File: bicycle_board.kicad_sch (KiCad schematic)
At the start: 47 parts, among them J1 Conn_02x05_Odd_Even, J10 USB_A, J11 Conn_01x02, J12 Conn_01x04, J13 Conn_01x04, J2 USB_C_Receptacle_USB2.0_16P, J5 Micro_SD_Card, J6 Conn_01x08, J7 Conn_01x03, J8 Conn_01x02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

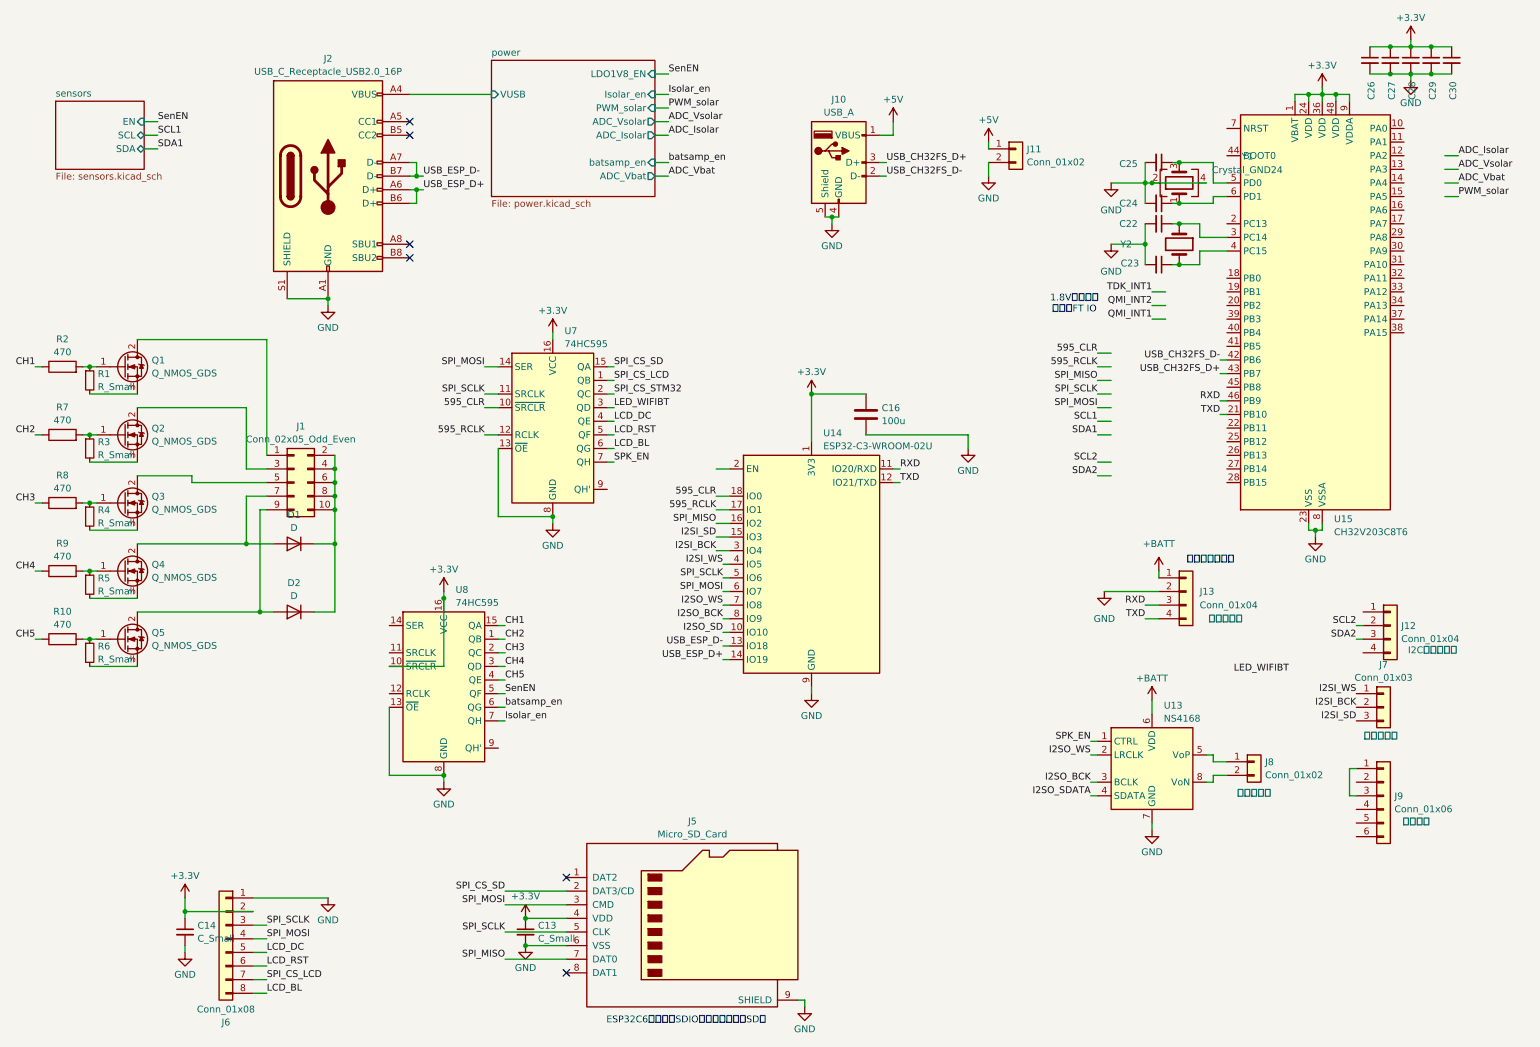
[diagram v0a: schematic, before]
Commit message: MOS管修改为GSD, 添加芯片附近滤波电容、上拉电阻等，调整模块间布局，改正AHT20封装，电解电容替换成1210 MLCC
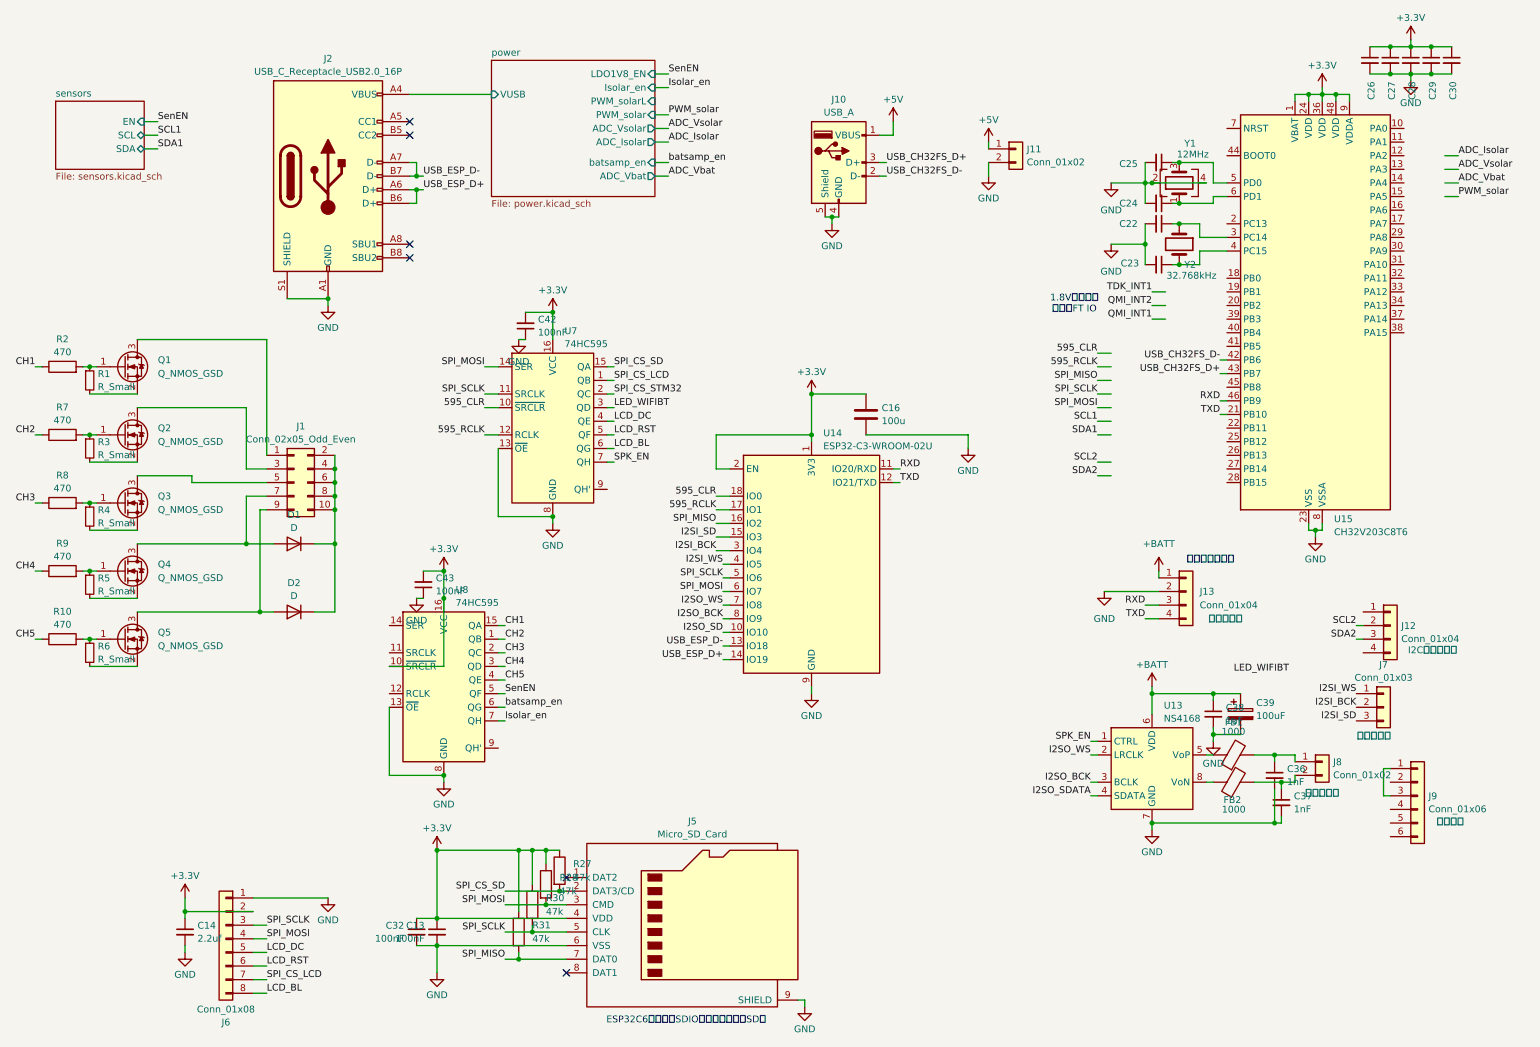
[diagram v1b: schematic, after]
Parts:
- added C32, C42, C43: 100nF, Capacitor_SMD:C_0402_1005Metric, symbol Device:C_Small
- added C36, C37: 1nF, Capacitor_SMD:C_0402_1005Metric, symbol Device:C_Small
- added C38: 1uF, Capacitor_SMD:C_0402_1005Metric, symbol Device:C_Small
- added C39: 100uF, Capacitor_SMD:C_1210_3225Metric, symbol Device:C_Polarized
- added FB1, FB2: 1000, Inductor_SMD:L_0805_2012Metric, symbol Device:FerriteBead
- added R27, R28, R30, R31: 47k, Resistor_SMD:R_0402_1005Metric, symbol Device:R
- C13, C26, C27, C28, C29, C30: value C_Small -> 100nF
- C14: value C_Small -> 2.2uf; footprint Capacitor_SMD:C_0402_1005Metric -> Capacitor_SMD:C_0603_1608Metric
- Q1, Q2, Q3, Q4, Q5: value Q_NMOS_GDS -> Q_NMOS_GSD; symbol Device:Q_NMOS_GDS -> Device:Q_NMOS_GSD
- Y1: value Crystal_GND24 -> 12MHz
- Y2: value Crystal -> 32.768kHz
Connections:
- net +3.3V: now also U14.2 (EN), C32.1, C42.2, C43.2, R27.1, R28.1, R30.1, R31.1
- net +BATT: now also C38.1, C39.1
- net GND: now also C32.2, C36.2, C37.2, C38.2, C39.2, C42.1, C43.1
- net SPI_CS_SD: now also R27.2
- net SPI_MISO: now also R31.2
- net SPI_MOSI: now also R28.2
- net SPI_SCLK: now also R30.2
- net at R1.2: now also Q1.2 (S); no longer Q1.3 (S)
- net at D1.2 (A), J1.7 (Pin_7): now also Q4.3 (D); no longer Q4.2 (D)
- net at R6.2: now also Q5.2 (S); no longer Q5.3 (S)
- net at Q3.2 (S): now also R4.2; no longer J1.5 (Pin_5)
- net at Q3.3 (D): now also J1.5 (Pin_5); no longer R4.2
- net at J1.1 (Pin_1): now also Q1.3 (D); no longer Q1.2 (D)
- net at R5.2: now also Q4.2 (S); no longer Q4.3 (S)
- net at U13.5 (VoP): now also FB1.1; no longer J8.1 (Pin_1)
- net at U13.8 (VoN): now also FB2.1; no longer J8.2 (Pin_2)
- net at D2.2 (A), J1.9 (Pin_9): now also Q5.3 (D); no longer Q5.2 (D)
- net at R3.2: now also Q2.2 (S); no longer Q2.3 (S)
- net at J1.3 (Pin_3): now also Q2.3 (D); no longer Q2.2 (D)
- new net: C37.1, FB2.2, J8.2 (Pin_2)
- new net: C36.1, FB1.2, J8.1 (Pin_1)
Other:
- sheet power ports: added PWM_solarL; removed none
- moved on the sheet: C13, J8, J9

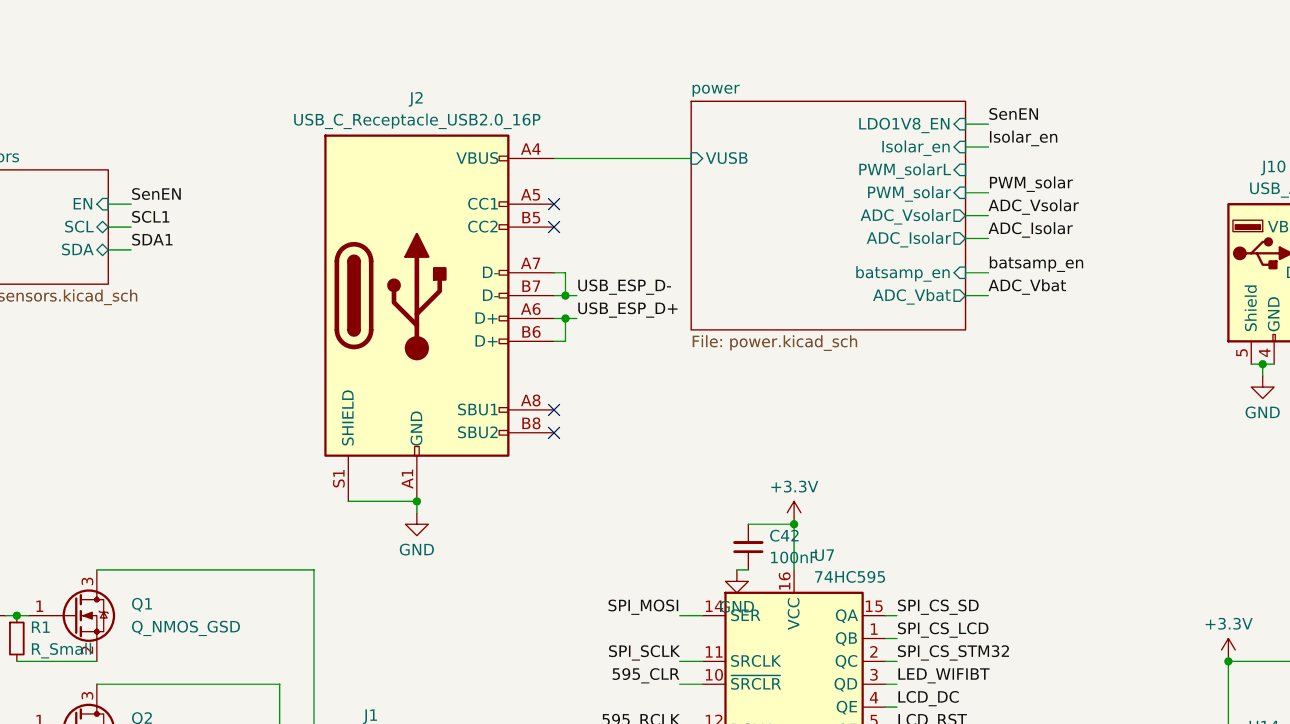
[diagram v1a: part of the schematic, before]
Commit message: 添加升压USB 5V输出
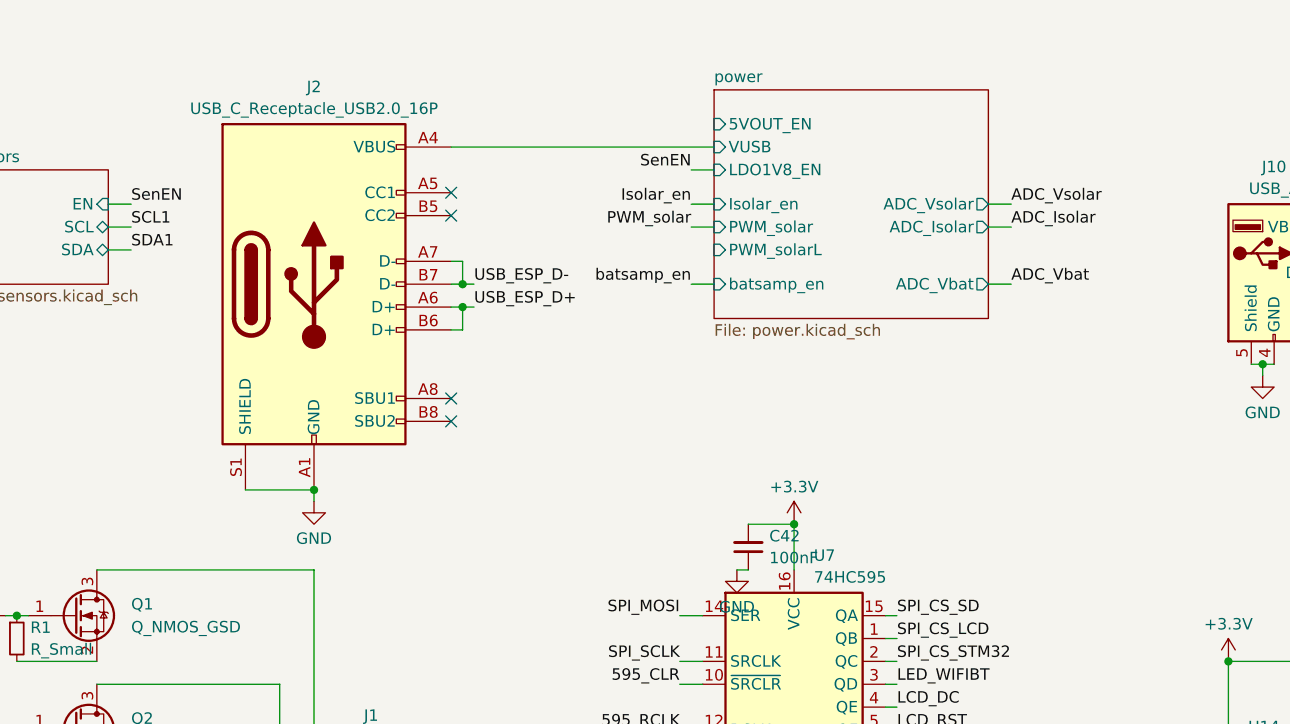
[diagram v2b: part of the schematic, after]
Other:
- sheet power ports: added 5VOUT_EN; removed none
- moved on the sheet: J2

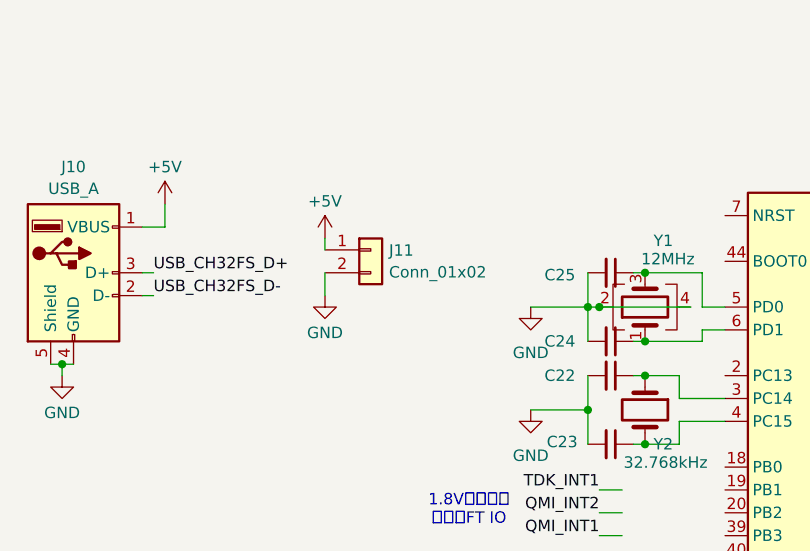
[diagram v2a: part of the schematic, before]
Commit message: 初步划定PCB边缘，改为紧凑布局
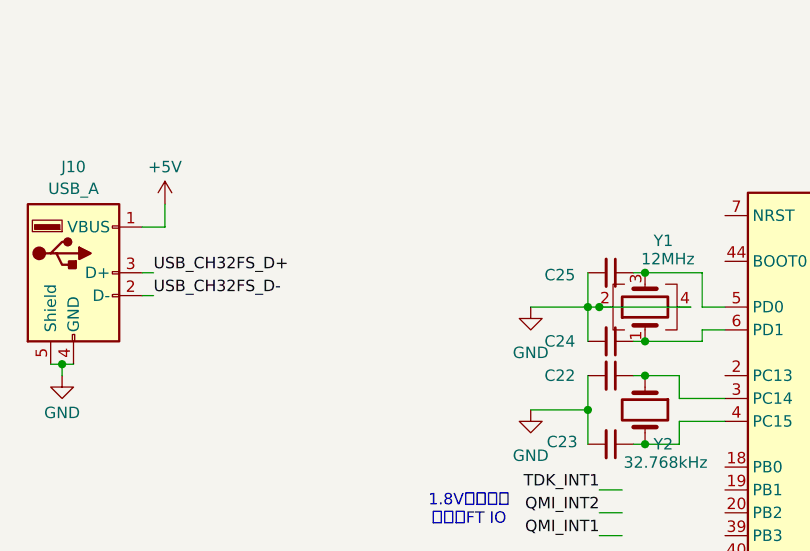
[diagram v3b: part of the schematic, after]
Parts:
- removed J11: Conn_01x02, Connector_PinHeader_2.54mm:PinHeader_1x02_P2.54mm_Vertical, symbol Connector_Generic:Conn_01x02
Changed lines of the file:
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@@
 	(wire
 		(pts
-			(xy 196.85 31.75) (xy 196.85 33.02)
-		)
-		(stroke
-			(width 0)
-			(type default)
-		)
-	)
-	(wire
-		(pts
 			(xy 238.76 146.05) (xy 237.49 146.05)
 		)
@@
 	(wire
 		(pts
-			(xy 196.85 35.56) (xy 196.85 38.1)
-		)
-		(stroke
-			(width 0)
-			(type default)
-		)
-	)
-	(wire
-		(pts
 			(xy 167.64 45.72) (xy 167.64 46.99)
 		)
@@
 	)
 	(symbol
-		(lib_id "Connector_Generic:Conn_01x02")
-		(at 201.93 33.02 0)
-		(unit 1)
-		(exclude_from_sim no)
-		(in_bom yes)
-		(on_board yes)
-		(dnp no)
-		(fields_autoplaced yes)
-		(property "Reference" "J11"
-			(at 203.962 33.0778 0)
-			(effects
-				(font
-					(size 1.27 1.27)
-				)
-				(justify left)
-			)
-		)
-		(property "Value" "Conn_01x02"
-			(at 203.962 35.5021 0)
-			(effects
-				(font
-					(size 1.27 1.27)
-				)
-				(justify left)
-			)
-		)
-		(property "Footprint" "Connector_PinHeader_2.54mm:PinHeader_1x02_P2.54mm_Vertical"
-			(at 201.93 33.02 0)
-			(effects
-				(font
-					(size 1.27 1.27)
-				)
-				(hide yes)
-			)
-		)
-		(property "Datasheet" "~"
-			(at 201.93 33.02 0)
-			(effects
-				(font
-					(size 1.27 1.27)
-				)
-				(hide yes)
-			)
-		)
-		(property "Description" "5V电源输出"
-			(at 201.93 33.02 0)
-			(effects
-				(font
-					(size 1.27 1.27)
-				)
-				(hide yes)
-			)
-		)
-		(property "Sim.Type" ""
-			(at 201.93 33.02 0)
-			(effects
-				(font
-					(size 1.27 1.27)
-				)
-				(hide yes)
-			)
-		)
-		(pin "2"
-		)
-		(pin "1"
-		)
-		(instances
-			(project ""
-				(path "/a369956d-4c9f-46c3-810f-e3e9616ab1a2"
-					(reference "J11")
-					(unit 1)
-				)
-			)
-		)
-	)
-	(symbol
 		(lib_id "RF_Module:ESP32-C3-WROOM-02U")
 		(at 163.83 110.49 0)
@@
 	)
 	(symbol
-		(lib_id "power:GND")
-		(at 196.85 38.1 0)
-		(unit 1)
-		(exclude_from_sim no)
-		(in_bom yes)
-		(on_board yes)
-		(dnp no)
-		(fields_autoplaced yes)
-		(property "Reference" "#PWR048"
-			(at 196.85 44.45 0)
-			(effects
-				(font
-					(size 1.27 1.27)
-				)
-				(hide yes)
-			)
-		)
-		(property "Value" "GND"
-			(at 196.85 42.2331 0)
-			(effects
-				(font
-					(size 1.27 1.27)
-				)
-			)
-		)
-		(property "Footprint" ""
-			(at 196.85 38.1 0)
-			(effects
-				(font
-					(size 1.27 1.27)
-				)
-				(hide yes)
-			)
-		)
-		(property "Datasheet" ""
-			(at 196.85 38.1 0)
-			(effects
-				(font
-					(size 1.27 1.27)
-				)
-				(hide yes)
-			)
-		)
-		(property "Description" "Power symbol creates a global label with name \"GND\" , ground"
-			(at 196.85 38.1 0)
-			(effects
-				(font
-					(size 1.27 1.27)
-				)
-				(hide yes)
-			)
-		)
-		(pin "1"
-		)
-		(instances
-			(project "bicycle_board"
-				(path "/a369956d-4c9f-46c3-810f-e3e9616ab1a2"
-					(reference "#PWR048")
-					(unit 1)
-				)
-			)
-		)
-	)
-	(symbol
 		(lib_id "Device:FerriteBead")
 		(at 242.57 151.13 90)
@@
 					(unit 1)
 				)
-			)
-		)
-	)
-	(symbol
-		(lib_id "power:+5V")
-		(at 196.85 31.75 0)
-		(unit 1)
-		(exclude_from_sim no)
-		(in_bom yes)
-		(on_board yes)
-		(dnp no)
-		(fields_autoplaced yes)
-		(property "Reference" "#PWR051"
-			(at 196.85 35.56 0)
-			(effects
-				(font
-					(size 1.27 1.27)
-				)
-				(hide yes)
-			)
-		)
-		(property "Value" "+5V"
-			(at 196.85 27.6169 0)
-			(effects
-				(font
-					(size 1.27 1.27)
-				)
-			)
-		)
-		(property "Footprint" ""
-			(at 196.85 31.75 0)
-			(effects
-				(font
-					(size 1.27 1.27)
-				)
-				(hide yes)
-			)
-		)
-		(property "Datasheet" ""
-			(at 196.85 31.75 0)
-			(effects
-				(font
-					(size 1.27 1.27)
-				)
-				(hide yes)
-			)
-		)
-		(property "Description" "Power symbol creates a global label with name \"+5V\""
-			(at 196.85 31.75 0)
-			(effects
-				(font
-					(size 1.27 1.27)
-				)
-				(hide yes)
-			)
-		)
-		(pin "1"
-		)
-		(instances
-			(project "bicycle_board"
-				(path "/a369956d-4c9f-46c3-810f-e3e9616ab1a2"
-					(reference "#PWR051")
-					(unit 1)
-				)
